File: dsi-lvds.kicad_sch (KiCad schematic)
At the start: 19 parts, among them U16 SN65DSI84

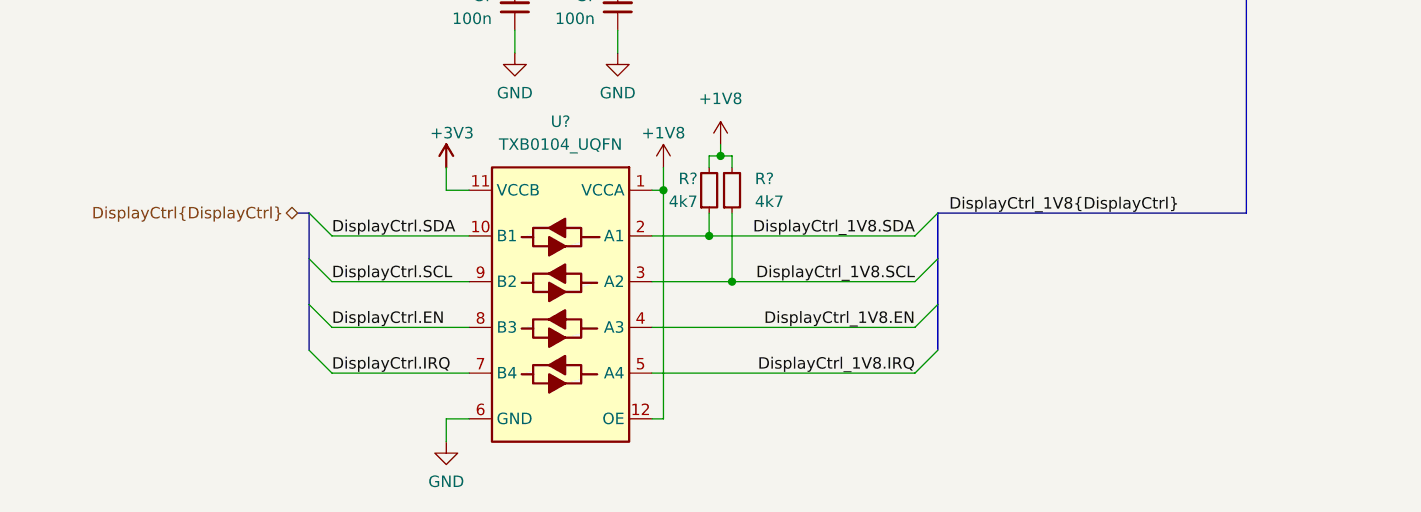
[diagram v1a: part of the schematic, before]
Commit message: [#54932] Remove DSI conn; Add AntmUD conn; Rename buses
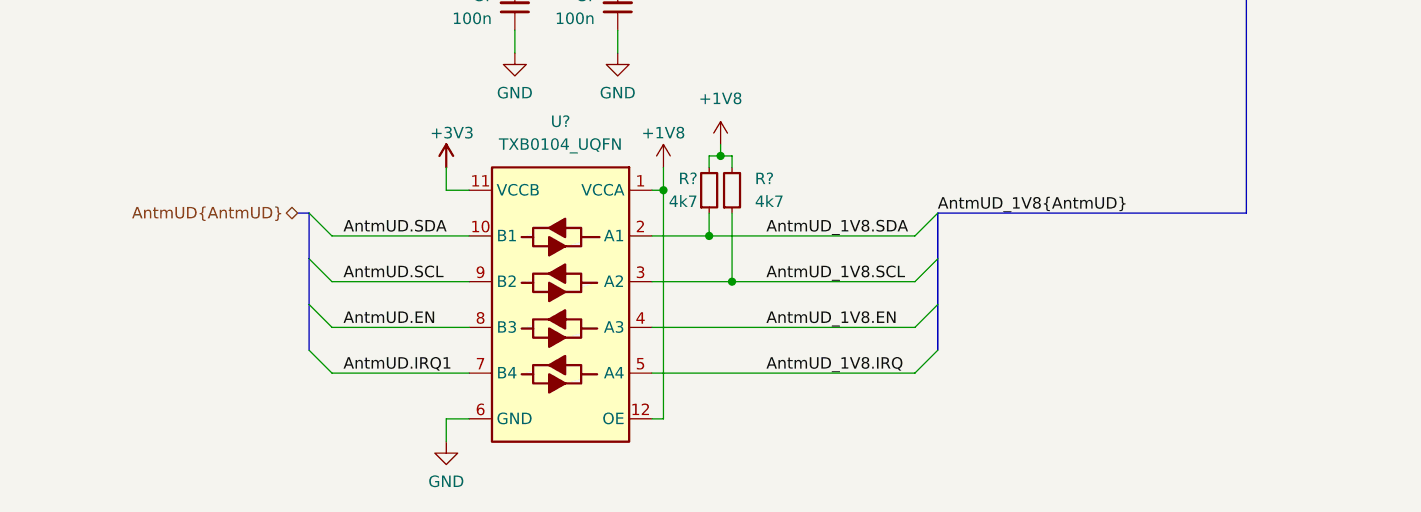
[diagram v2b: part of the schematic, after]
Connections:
- net DisplayCtrl_1V8.EN: no longer U?.4 (A3)
- net DisplayCtrl_1V8.IRQ: no longer U?.5 (A4)
- net DisplayCtrl_1V8.SCL: no longer R?.1, U?.3 (A2)
- net DisplayCtrl_1V8.SDA: no longer R?.1, U?.2 (A1)
- net DisplayCtrl.EN renamed AntmUD.EN
- net DisplayCtrl.IRQ renamed AntmUD.IRQ1
- net DisplayCtrl.SCL renamed AntmUD.SCL
- net DisplayCtrl.SDA renamed AntmUD.SDA
- new net AntmUD_1V8.EN: U?.4 (A3)
- new net AntmUD_1V8.IRQ: U?.5 (A4)
- new net AntmUD_1V8.SCL: R?.1, U?.3 (A2)
- new net AntmUD_1V8.SDA: R?.1, U?.2 (A1)

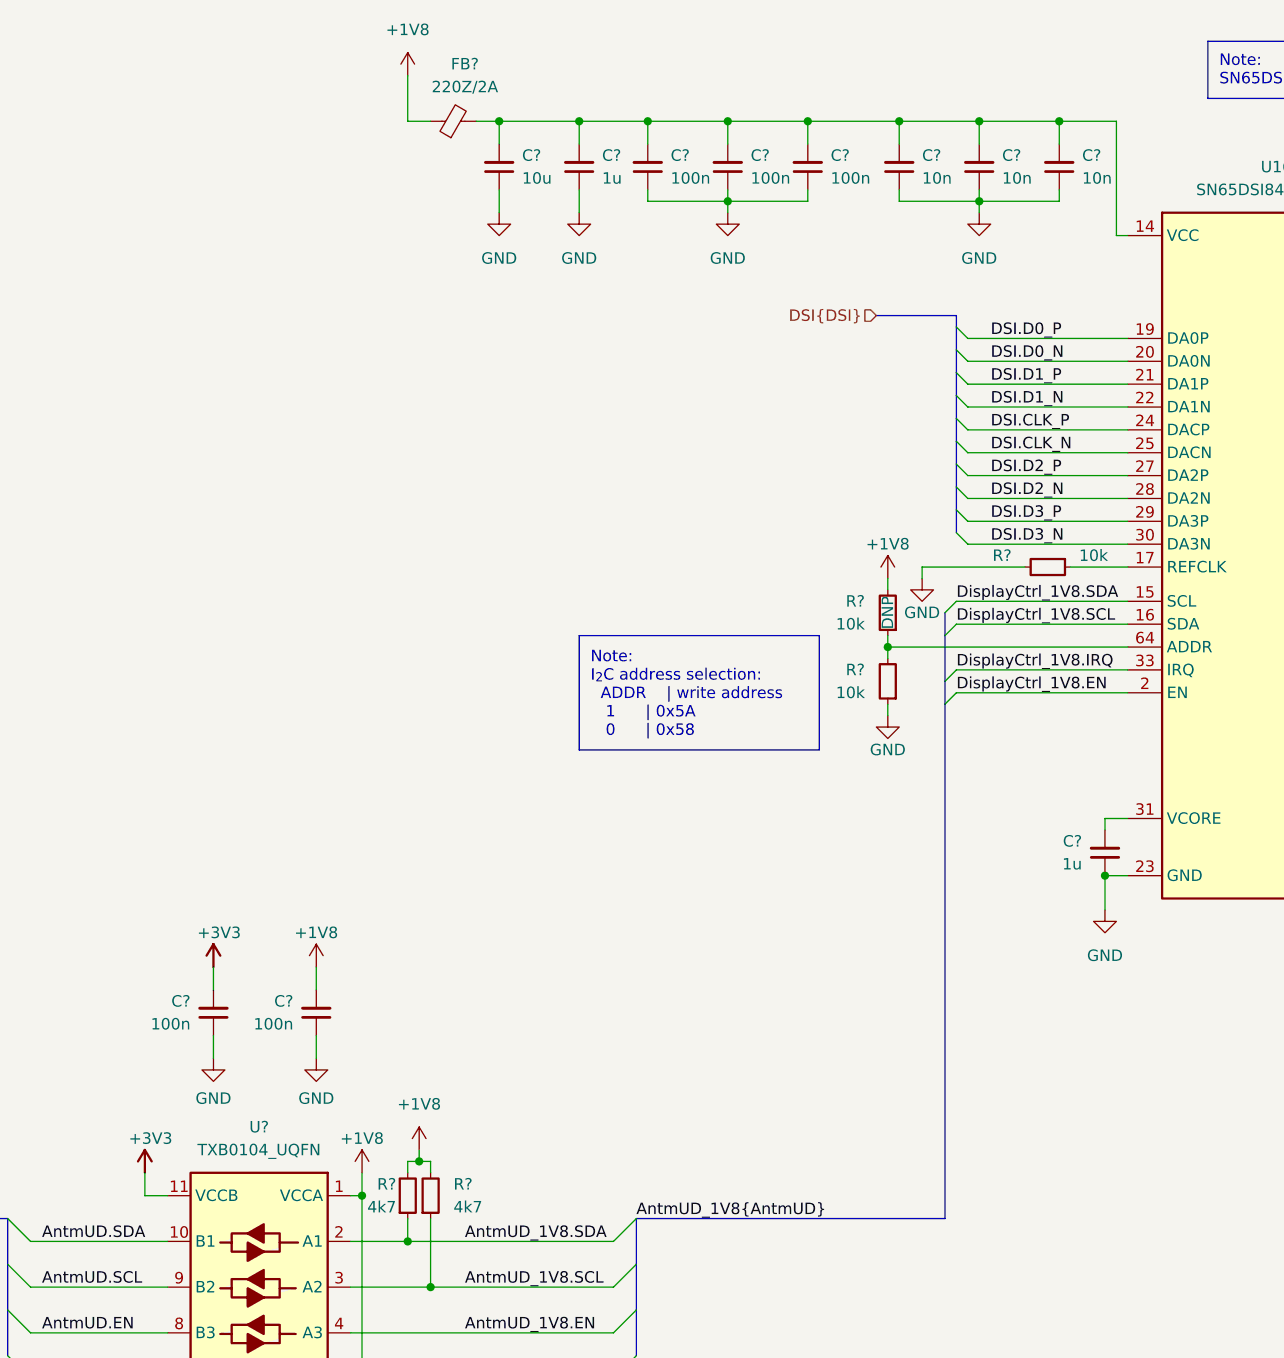
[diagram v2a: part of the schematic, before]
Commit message: [#54932] Reanotate schematics; Propagate component changes to PCB
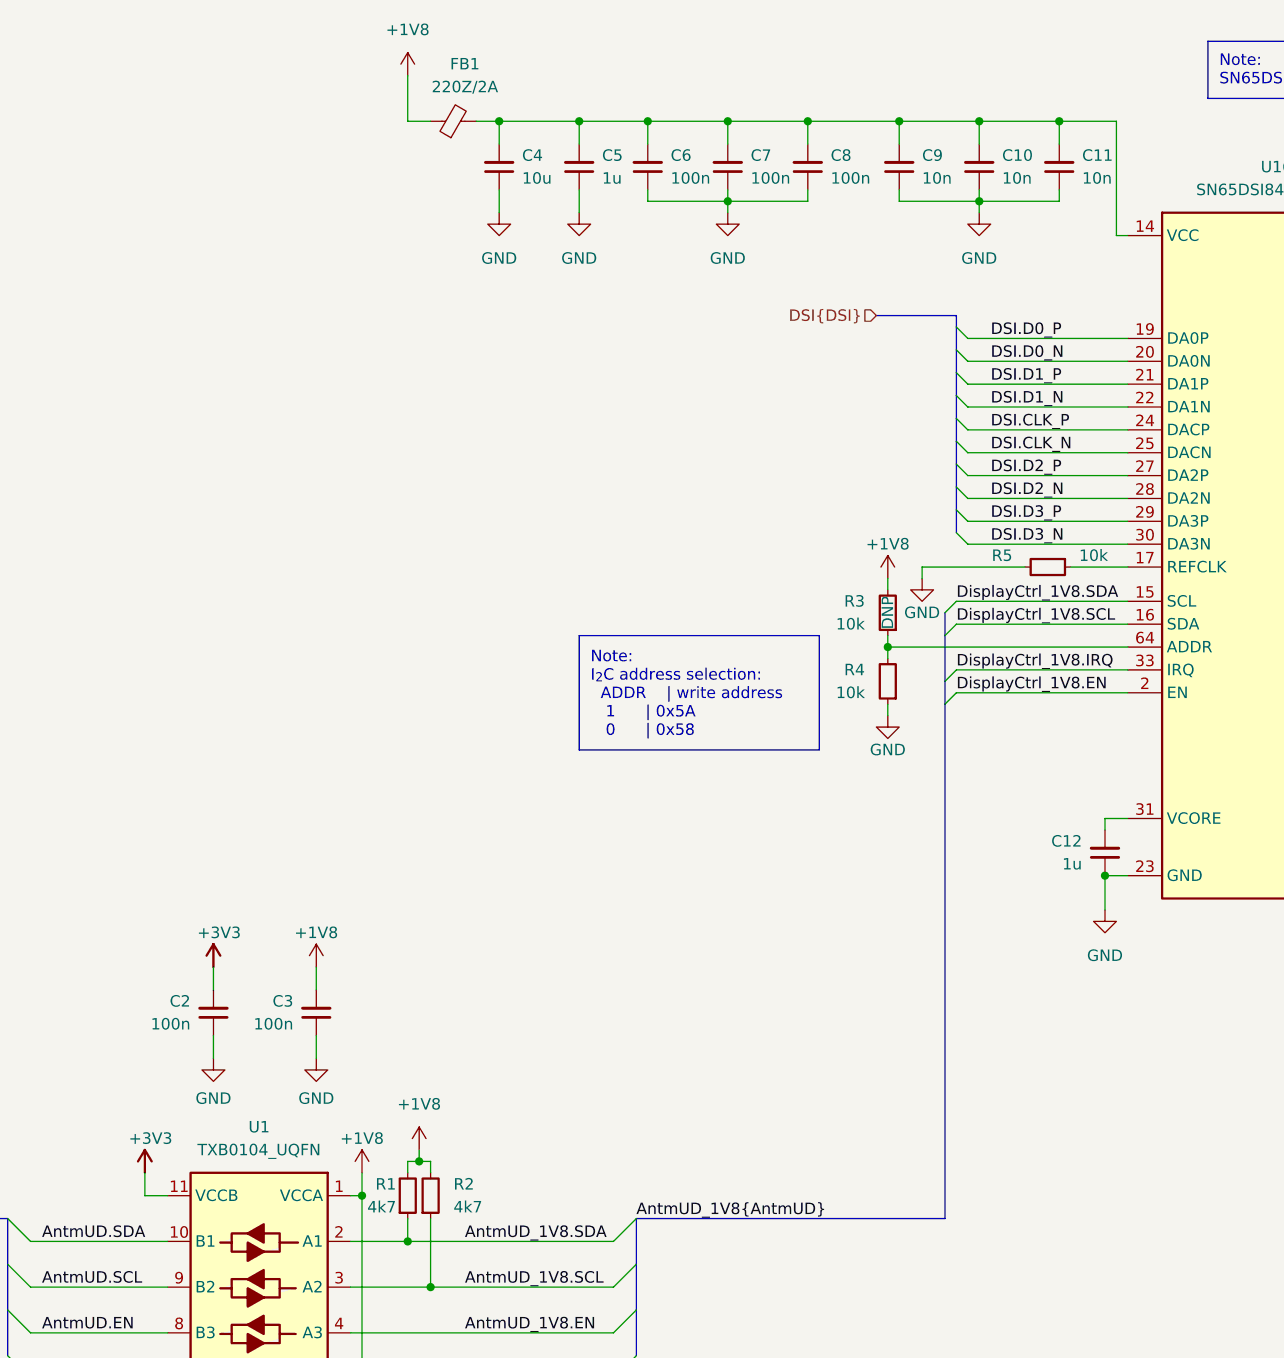
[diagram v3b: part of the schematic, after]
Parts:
- gave numbers to parts that had none: 18
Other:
- title: CM4 Baseboard -> CM4 Baseboard LVDS Adapter
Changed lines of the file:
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@@
   (paper "A3")
   (title_block
-    (title "CM4 Baseboard")
+    (title "CM4 Baseboard LVDS Adapter")
     (rev "1.0.0")
     (company "Antmicro")
@@
       (project "cm4-lvds-adapter"
         (path "/60b842dc-0853-4a25-99ac-5784ddf94d0d/420ebe12-f825-449a-8afd-25702eb411ad"
-          (reference "C?") (unit 1)
+          (reference "C12") (unit 1)
         )
       )
@@
       (project "cm4-lvds-adapter"
         (path "/60b842dc-0853-4a25-99ac-5784ddf94d0d/420ebe12-f825-449a-8afd-25702eb411ad"
-          (reference "C?") (unit 1)
+          (reference "C3") (unit 1)
         )
       )
@@
       (project "cm4-lvds-adapter"
         (path "/60b842dc-0853-4a25-99ac-5784ddf94d0d/420ebe12-f825-449a-8afd-25702eb411ad"
-          (reference "U16") (unit 1)
+          (reference "U2") (unit 1)
         )
       )
@@
       (project "cm4-lvds-adapter"
         (path "/60b842dc-0853-4a25-99ac-5784ddf94d0d/420ebe12-f825-449a-8afd-25702eb411ad"
-          (reference "C?") (unit 1)
+          (reference "C8") (unit 1)
         )
       )
@@
       (project "cm4-lvds-adapter"
         (path "/60b842dc-0853-4a25-99ac-5784ddf94d0d/420ebe12-f825-449a-8afd-25702eb411ad"
-          (reference "C?") (unit 1)
+          (reference "C11") (unit 1)
         )
       )
@@
       (project "cm4-lvds-adapter"
         (path "/60b842dc-0853-4a25-99ac-5784ddf94d0d/420ebe12-f825-449a-8afd-25702eb411ad"
-          (reference "#PWR0109") (unit 1)
+          (reference "#PWR014") (unit 1)
         )
       )
@@
       (project "cm4-lvds-adapter"
         (path "/60b842dc-0853-4a25-99ac-5784ddf94d0d/420ebe12-f825-449a-8afd-25702eb411ad"
-          (reference "FB?") (unit 1)
+          (reference "FB1") (unit 1)
         )
       )
@@
       (project "cm4-lvds-adapter"
         (path "/60b842dc-0853-4a25-99ac-5784ddf94d0d/420ebe12-f825-449a-8afd-25702eb411ad"
-          (reference "#PWR0103") (unit 1)
+          (reference "#PWR026") (unit 1)
         )
       )
@@
       (project "cm4-lvds-adapter"
         (path "/60b842dc-0853-4a25-99ac-5784ddf94d0d/420ebe12-f825-449a-8afd-25702eb411ad"
-          (reference "#PWR0115") (unit 1)
+          (reference "#PWR019") (unit 1)
         )
       )
@@
       (project "cm4-lvds-adapter"
         (path "/60b842dc-0853-4a25-99ac-5784ddf94d0d/420ebe12-f825-449a-8afd-25702eb411ad"
-          (reference "#PWR0110") (unit 1)
+          (reference "#PWR012") (unit 1)
         )
       )
@@
       (project "cm4-lvds-adapter"
         (path "/60b842dc-0853-4a25-99ac-5784ddf94d0d/420ebe12-f825-449a-8afd-25702eb411ad"
-          (reference "C?") (unit 1)
+          (reference "C4") (unit 1)
         )
       )
@@
       (project "cm4-lvds-adapter"
         (path "/60b842dc-0853-4a25-99ac-5784ddf94d0d/420ebe12-f825-449a-8afd-25702eb411ad"
-          (reference "#PWR0114") (unit 1)
+          (reference "#PWR022") (unit 1)
         )
       )
@@
       (project "cm4-lvds-adapter"
         (path "/60b842dc-0853-4a25-99ac-5784ddf94d0d/420ebe12-f825-449a-8afd-25702eb411ad"
-          (reference "R?") (unit 1)
+          (reference "R3") (unit 1)
         )
       )
@@
       (project "cm4-lvds-adapter"
         (path "/60b842dc-0853-4a25-99ac-5784ddf94d0d/420ebe12-f825-449a-8afd-25702eb411ad"
-          (reference "C?") (unit 1)
+          (reference "C2") (unit 1)
         )
       )
@@
       (project "cm4-lvds-adapter"
         (path "/60b842dc-0853-4a25-99ac-5784ddf94d0d/420ebe12-f825-449a-8afd-25702eb411ad"
-          (reference "R?") (unit 1)
+          (reference "R5") (unit 1)
         )
       )
@@
       (project "cm4-lvds-adapter"
         (path "/60b842dc-0853-4a25-99ac-5784ddf94d0d/420ebe12-f825-449a-8afd-25702eb411ad"
-          (reference "#PWR0105") (unit 1)
+          (reference "#PWR028") (unit 1)
         )
       )
@@
       (project "cm4-lvds-adapter"
         (path "/60b842dc-0853-4a25-99ac-5784ddf94d0d/420ebe12-f825-449a-8afd-25702eb411ad"
-          (reference "#PWR0111") (unit 1)
+          (reference "#PWR015") (unit 1)
         )
       )
@@
       (project "cm4-lvds-adapter"
         (path "/60b842dc-0853-4a25-99ac-5784ddf94d0d/420ebe12-f825-449a-8afd-25702eb411ad"
-          (reference "#PWR0116") (unit 1)
+          (reference "#PWR023") (unit 1)
         )
       )
@@
       (project "cm4-lvds-adapter"
         (path "/60b842dc-0853-4a25-99ac-5784ddf94d0d/420ebe12-f825-449a-8afd-25702eb411ad"
-          (reference "C?") (unit 1)
+          (reference "C9") (unit 1)
         )
       )
@@
       (project "cm4-lvds-adapter"
         (path "/60b842dc-0853-4a25-99ac-5784ddf94d0d/420ebe12-f825-449a-8afd-25702eb411ad"
-          (reference "#PWR0108") (unit 1)
+          (reference "#PWR016") (unit 1)
         )
       )
@@
       (project "cm4-lvds-adapter"
         (path "/60b842dc-0853-4a25-99ac-5784ddf94d0d/420ebe12-f825-449a-8afd-25702eb411ad"
-          (reference "#PWR0112") (unit 1)
+          (reference "#PWR017") (unit 1)
         )
       )
@@
       (project "cm4-lvds-adapter"
         (path "/60b842dc-0853-4a25-99ac-5784ddf94d0d/420ebe12-f825-449a-8afd-25702eb411ad"
-          (reference "C?") (unit 1)
+          (reference "C7") (unit 1)
         )
       )
@@
       (project "cm4-lvds-adapter"
         (path "/60b842dc-0853-4a25-99ac-5784ddf94d0d/420ebe12-f825-449a-8afd-25702eb411ad"
-          (reference "C?") (unit 1)
+          (reference "C5") (unit 1)
         )
       )
@@
       (project "cm4-lvds-adapter"
         (path "/60b842dc-0853-4a25-99ac-5784ddf94d0d/420ebe12-f825-449a-8afd-25702eb411ad"
-          (reference "R?") (unit 1)
+          (reference "R1") (unit 1)
         )
       )
@@
       (project "cm4-lvds-adapter"
         (path "/60b842dc-0853-4a25-99ac-5784ddf94d0d/420ebe12-f825-449a-8afd-25702eb411ad"
-          (reference "#PWR0102") (unit 1)
+          (reference "#PWR024") (unit 1)
         )
       )
@@
       (project "cm4-lvds-adapter"
         (path "/60b842dc-0853-4a25-99ac-5784ddf94d0d/420ebe12-f825-449a-8afd-25702eb411ad"
-          (reference "U?") (unit 1)
+          (reference "U1") (unit 1)
         )
       )
@@
       (project "cm4-lvds-adapter"
         (path "/60b842dc-0853-4a25-99ac-5784ddf94d0d/420ebe12-f825-449a-8afd-25702eb411ad"
-          (reference "#PWR0107") (unit 1)
+          (reference "#PWR018") (unit 1)
         )
       )
@@
       (project "cm4-lvds-adapter"
         (path "/60b842dc-0853-4a25-99ac-5784ddf94d0d/420ebe12-f825-449a-8afd-25702eb411ad"
-          (reference "C?") (unit 1)
+          (reference "C10") (unit 1)
         )
       )
@@
       (project "cm4-lvds-adapter"
         (path "/60b842dc-0853-4a25-99ac-5784ddf94d0d/420ebe12-f825-449a-8afd-25702eb411ad"
-          (reference "C?") (unit 1)
+          (reference "C6") (unit 1)
         )
       )
@@
       (project "cm4-lvds-adapter"
         (path "/60b842dc-0853-4a25-99ac-5784ddf94d0d/420ebe12-f825-449a-8afd-25702eb411ad"
-          (reference "#PWR0104") (unit 1)
+          (reference "#PWR027") (unit 1)
         )
       )
@@
       (project "cm4-lvds-adapter"
         (path "/60b842dc-0853-4a25-99ac-5784ddf94d0d/420ebe12-f825-449a-8afd-25702eb411ad"
-          (reference "#PWR0106") (unit 1)
+          (reference "#PWR020") (unit 1)
         )
       )
@@
       (project "cm4-lvds-adapter"
         (path "/60b842dc-0853-4a25-99ac-5784ddf94d0d/420ebe12-f825-449a-8afd-25702eb411ad"
-          (reference "#PWR0117") (unit 1)
+          (reference "#PWR013") (unit 1)
         )
       )
@@
       (project "cm4-lvds-adapter"
         (path "/60b842dc-0853-4a25-99ac-5784ddf94d0d/420ebe12-f825-449a-8afd-25702eb411ad"
-          (reference "R?") (unit 1)
+          (reference "R2") (unit 1)
         )
       )
@@
       (project "cm4-lvds-adapter"
         (path "/60b842dc-0853-4a25-99ac-5784ddf94d0d/420ebe12-f825-449a-8afd-25702eb411ad"
-          (reference "R?") (unit 1)
+          (reference "R4") (unit 1)
         )
       )
@@
       (project "cm4-lvds-adapter"
         (path "/60b842dc-0853-4a25-99ac-5784ddf94d0d/420ebe12-f825-449a-8afd-25702eb411ad"
-          (reference "#PWR0113") (unit 1)
+          (reference "#PWR021") (unit 1)
         )
       )
@@
       (project "cm4-lvds-adapter"
         (path "/60b842dc-0853-4a25-99ac-5784ddf94d0d/420ebe12-f825-449a-8afd-25702eb411ad"
-          (reference "#PWR0101") (unit 1)
+          (reference "#PWR025") (unit 1)
         )
       )

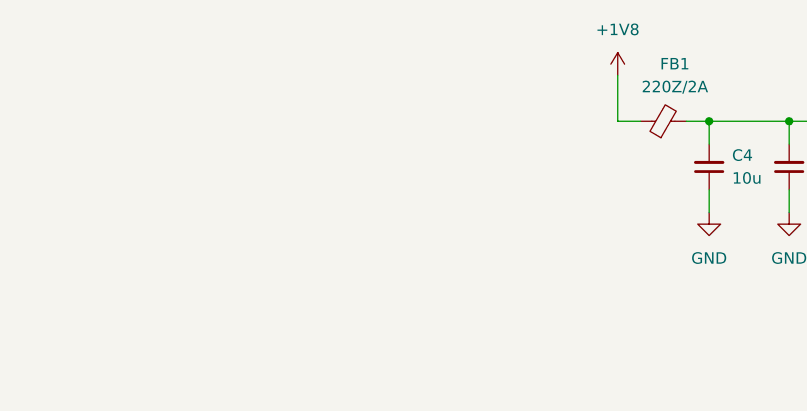
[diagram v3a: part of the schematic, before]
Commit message: [#54932] Add 1V8 LDO
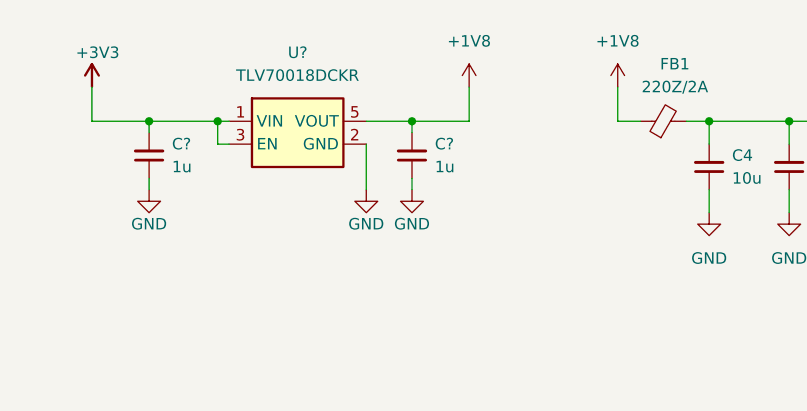
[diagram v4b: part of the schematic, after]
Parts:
- added C? (x2): C_1u_0402, antmicro-footprints:C_0402_1005Metric, symbol antmicroCapacitors0402:C_1u_0402
- added U?: TLV70018_SC70, antmicro-footprints:SC-70-5, symbol antmicroPMICVoltageRegulatorsLinear:TLV70018_SC70
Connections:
- net +1V8: now also C?.2, U?.5 (VOUT)
- net +3V3: now also C?.2, U?.1 (VIN), U?.3 (EN)
- net GND: now also C?.1, C?.1, U?.2 (GND)

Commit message: [#54932] Reanotate schematics
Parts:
- gave numbers to parts that had none: 3
- renumbered C8 to C10, C9 to C11, C10 to C12, C11 to C13, C12 to C14, C2 to C4, C3 to C5, C4 to C6, C5 to C7, C6 to C8, C7 to C9, U1 to U2
